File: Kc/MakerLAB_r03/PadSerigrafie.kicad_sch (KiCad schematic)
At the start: 5 parts

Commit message: Power Supply
Seconda fase
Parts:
- added TP20: Potenziometer, MountingHole:MountingHole_6.5mm_Pad_Via, symbol Connector:TestPoint
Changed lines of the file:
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@@
+    (pin "1")
+  )
+  (symbol (lib_id "Connector:TestPoint") (at 39.37 97.79 0) (unit 1)
+    (in_bom yes) (on_board yes) (fields_autoplaced)
+    (property "Reference" "TP20" (id 0) (at 41.91 93.2179 0)
+      (effects (font (size 1.27 1.27)) (justify left))
+    )
+    (property "Value" "Potenziometer" (id 1) (at 41.91 95.7579 0)
+      (effects (font (size 1.27 1.27)) (justify left))
+    )
+    (property "Footprint" "MountingHole:MountingHole_6.5mm_Pad_Via" (id 2) (at 44.45 97.79 0)
+      (effects (font (size 1.27 1.27)) hide)
+    )
+    (property "Datasheet" "~" (id 3) (at 44.45 97.79 0)
+      (effects (font (size 1.27 1.27)) hide)
+    )
     (pin "1")
   )

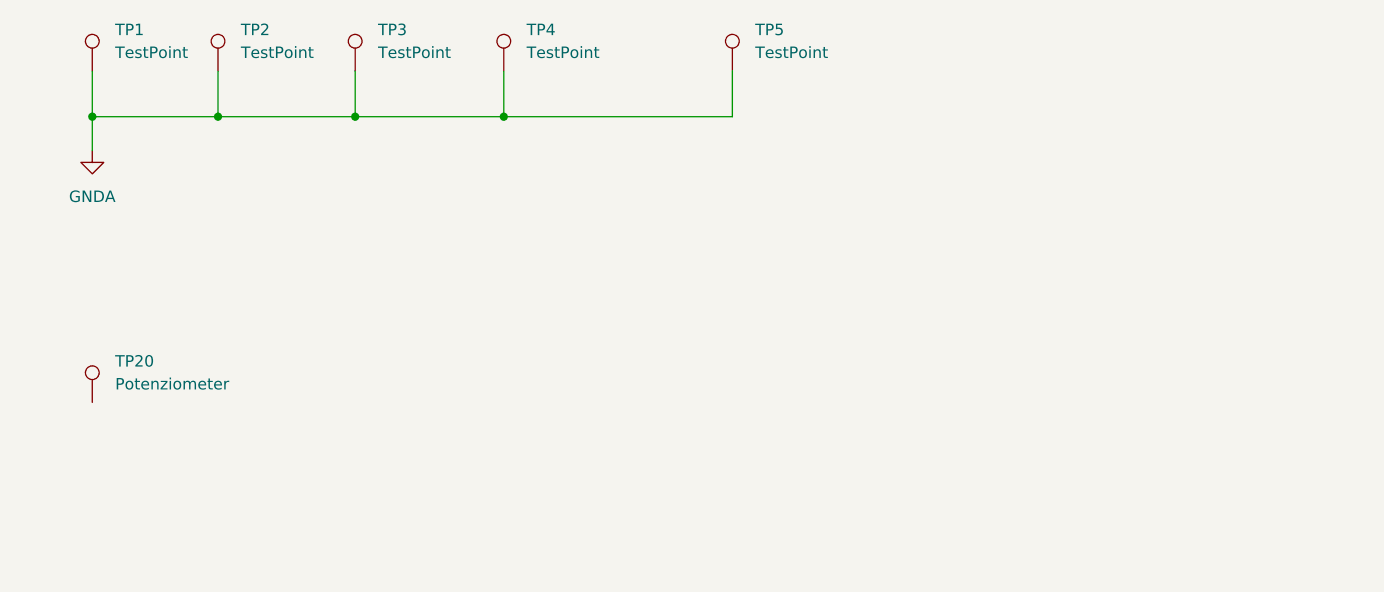
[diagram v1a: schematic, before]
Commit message: Layout Alimentatori OK
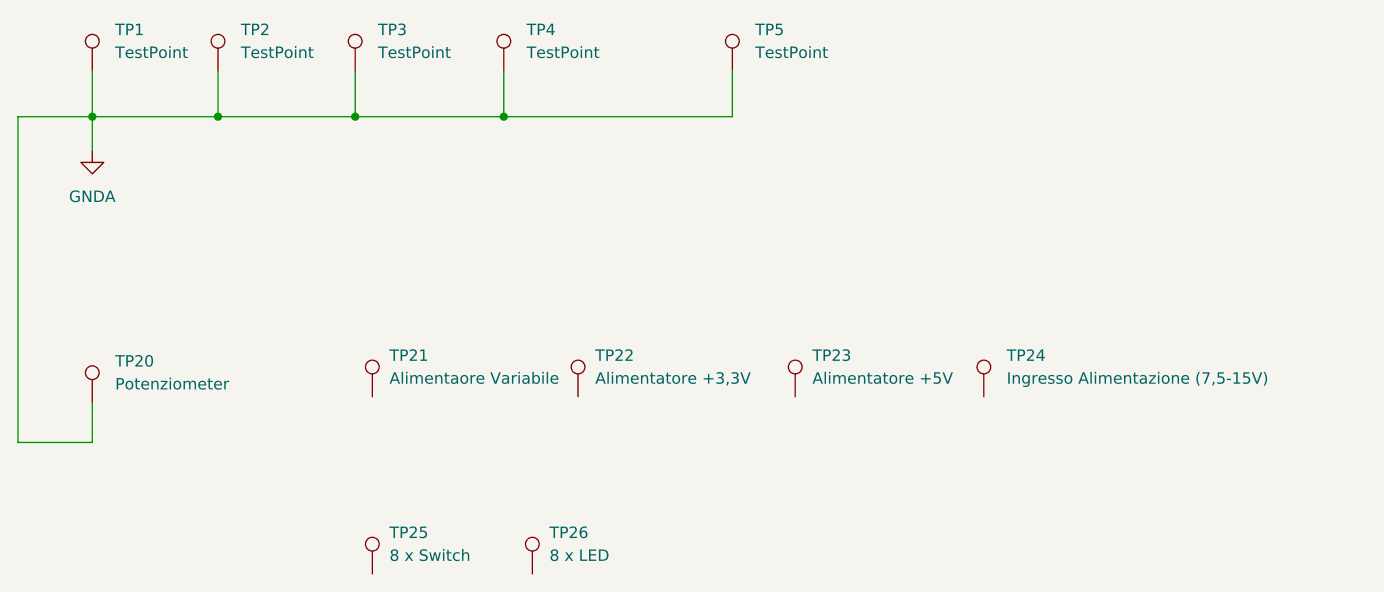
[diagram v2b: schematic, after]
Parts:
- added TP21: Alimentaore Variabile, Symbol:Alimentatore Variabile, symbol Connector:TestPoint
- added TP22: Alimentatore +3,3V, Symbol:Alimentatore Variabile, symbol Connector:TestPoint
- added TP23: Alimentatore +5V, Symbol:Alimentatore Variabile, symbol Connector:TestPoint
- added TP24: Ingresso Alimentazione (7,5-15V), Symbol:Alimentatore Variabile, symbol Connector:TestPoint
- added TP25: 8 x Switch, Symbol:Alimentatore Variabile, symbol Connector:TestPoint
- added TP26: 8 x LED, Symbol:Alimentatore Variabile, symbol Connector:TestPoint
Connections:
- net GNDA: now also TP20.1
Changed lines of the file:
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@@
+    (stroke (width 0) (type default) (color 0 0 0 0))
+  )
+  (wire (pts (xy 31.115 66.04) (xy 39.37 66.04))
     (stroke (width 0) (type default) (color 0 0 0 0))
   )
@@
     (stroke (width 0) (type default) (color 0 0 0 0))
   )
+  (wire (pts (xy 39.37 97.79) (xy 39.37 102.235))
+    (stroke (width 0) (type default) (color 0 0 0 0))
+  )
   (wire (pts (xy 39.37 66.04) (xy 53.34 66.04))
     (stroke (width 0) (type default) (color 0 0 0 0))
   )
   (wire (pts (xy 53.34 66.04) (xy 68.58 66.04))
+    (stroke (width 0) (type default) (color 0 0 0 0))
+  )
+  (wire (pts (xy 31.115 102.235) (xy 31.115 66.04))
+    (stroke (width 0) (type default) (color 0 0 0 0))
+  )
+  (wire (pts (xy 39.37 102.235) (xy 31.115 102.235))
     (stroke (width 0) (type default) (color 0 0 0 0))
   )
@@
     (pin "1")
   )
+  (symbol (lib_id "Connector:TestPoint") (at 70.485 116.84 0) (unit 1)
+    (in_bom yes) (on_board yes) (fields_autoplaced)
+    (property "Reference" "TP25" (id 0) (at 72.39 112.2679 0)
+      (effects (font (size 1.27 1.27)) (justify left))
+    )
+    (property "Value" "8 x Switch" (id 1) (at 72.39 114.8079 0)
+      (effects (font (size 1.27 1.27)) (justify left))
+    )
+    (property "Footprint" "Symbol:Alimentatore Variabile" (id 2) (at 75.565 116.84 0)
+      (effects (font (size 1.27 1.27)) hide)
+    )
+    (property "Datasheet" "~" (id 3) (at 75.565 116.84 0)
+      (effects (font (size 1.27 1.27)) hide)
+    )
+    (pin "1")
+  )
   (symbol (lib_id "Connector:TestPoint") (at 39.37 97.79 0) (unit 1)
     (in_bom yes) (on_board yes) (fields_autoplaced)
@@
     (pin "1")
   )
+  (symbol (lib_id "Connector:TestPoint") (at 93.345 97.155 0) (unit 1)
+    (in_bom yes) (on_board yes) (fields_autoplaced)
+    (property "Reference" "TP22" (id 0) (at 95.25 92.5829 0)
+      (effects (font (size 1.27 1.27)) (justify left))
+    )
+    (property "Value" "Alimentatore +3,3V" (id 1) (at 95.25 95.1229 0)
+      (effects (font (size 1.27 1.27)) (justify left))
+    )
+    (property "Footprint" "Symbol:Alimentatore Variabile" (id 2) (at 98.425 97.155 0)
+      (effects (font (size 1.27 1.27)) hide)
+    )
+    (property "Datasheet" "~" (id 3) (at 98.425 97.155 0)
+      (effects (font (size 1.27 1.27)) hide)
+    )
+    (pin "1")
+  )
   (symbol (lib_id "Connector:TestPoint") (at 85.09 60.96 0) (unit 1)
     (in_bom yes) (on_board yes) (fields_autoplaced)
@@
     (pin "1")
   )
+  (symbol (lib_id "Connector:TestPoint") (at 138.43 97.155 0) (unit 1)
+    (in_bom yes) (on_board yes) (fields_autoplaced)
+    (property "Reference" "TP24" (id 0) (at 140.97 92.5829 0)
+      (effects (font (size 1.27 1.27)) (justify left))
+    )
+    (property "Value" "Ingresso Alimentazione (7,5-15V)" (id 1) (at 140.97 95.1229 0)
+      (effects (font (size 1.27 1.27)) (justify left))
+    )
+    (property "Footprint" "Symbol:Alimentatore Variabile" (id 2) (at 143.51 97.155 0)
+      (effects (font (size 1.27 1.27)) hide)
+    )
+    (property "Datasheet" "~" (id 3) (at 143.51 97.155 0)
+      (effects (font (size 1.27 1.27)) hide)
+    )
+    (pin "1")
+  )
+  (symbol (lib_id "Connector:TestPoint") (at 117.475 97.155 0) (unit 1)
+    (in_bom yes) (on_board yes) (fields_autoplaced)
+    (property "Reference" "TP23" (id 0) (at 119.38 92.5829 0)
+      (effects (font (size 1.27 1.27)) (justify left))
+    )
+    (property "Value" "Alimentatore +5V" (id 1) (at 119.38 95.1229 0)
+      (effects (font (size 1.27 1.27)) (justify left))
+    )
+    (property "Footprint" "Symbol:Alimentatore Variabile" (id 2) (at 122.555 97.155 0)
+      (effects (font (size 1.27 1.27)) hide)
+    )
+    (property "Datasheet" "~" (id 3) (at 122.555 97.155 0)
+      (effects (font (size 1.27 1.27)) hide)
+    )
+    (pin "1")
+  )
   (symbol (lib_id "Connector:TestPoint") (at 68.58 60.96 0) (unit 1)
     (in_bom yes) (on_board yes) (fields_autoplaced)
@@
     (pin "1")
   )
+  (symbol (lib_id "Connector:TestPoint") (at 88.265 116.84 0) (unit 1)
+    (in_bom yes) (on_board yes) (fields_autoplaced)
+    (property "Reference" "TP26" (id 0) (at 90.17 112.2679 0)
+      (effects (font (size 1.27 1.27)) (justify left))
+    )
+    (property "Value" "8 x LED" (id 1) (at 90.17 114.8079 0)
+      (effects (font (size 1.27 1.27)) (justify left))
+    )
+    (property "Footprint" "Symbol:Alimentatore Variabile" (id 2) (at 93.345 116.84 0)
+      (effects (font (size 1.27 1.27)) hide)
+    )
+    (property "Datasheet" "~" (id 3) (at 93.345 116.84 0)
+      (effects (font (size 1.27 1.27)) hide)
+    )
+    (pin "1")
+  )
   (symbol (lib_id "Connector:TestPoint") (at 53.34 60.96 0) (unit 1)
     (in_bom yes) (on_board yes) (fields_autoplaced)
@@
       (effects (font (size 1.27 1.27)) hide)
     )
+    (pin "1")
+  )
+  (symbol (lib_id "Connector:TestPoint") (at 70.485 97.155 0) (unit 1)
+    (in_bom yes) (on_board yes) (fields_autoplaced)
+    (property "Reference" "TP21" (id 0) (at 72.39 92.5829 0)
+      (effects (font (size 1.27 1.27)) (justify left))
+    )
+    (property "Value" "Alimentaore Variabile" (id 1) (at 72.39 95.1229 0)
+      (effects (font (size 1.27 1.27)) (justify left))
+    )
+    (property "Footprint" "Symbol:Alimentatore Variabile" (id 2) (at 75.565 97.155 0)
+      (effects (font (size 1.27 1.27)) hide)
+    )
+    (property "Datasheet" "~" (id 3) (at 75.565 97.155 0)
+      (effects (font (size 1.27 1.27)) hide)
+    )
